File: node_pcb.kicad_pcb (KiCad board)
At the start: 2 copper layers, 27.9 x 52.1 mm, 22 parts, among them J1 EXT_PWR

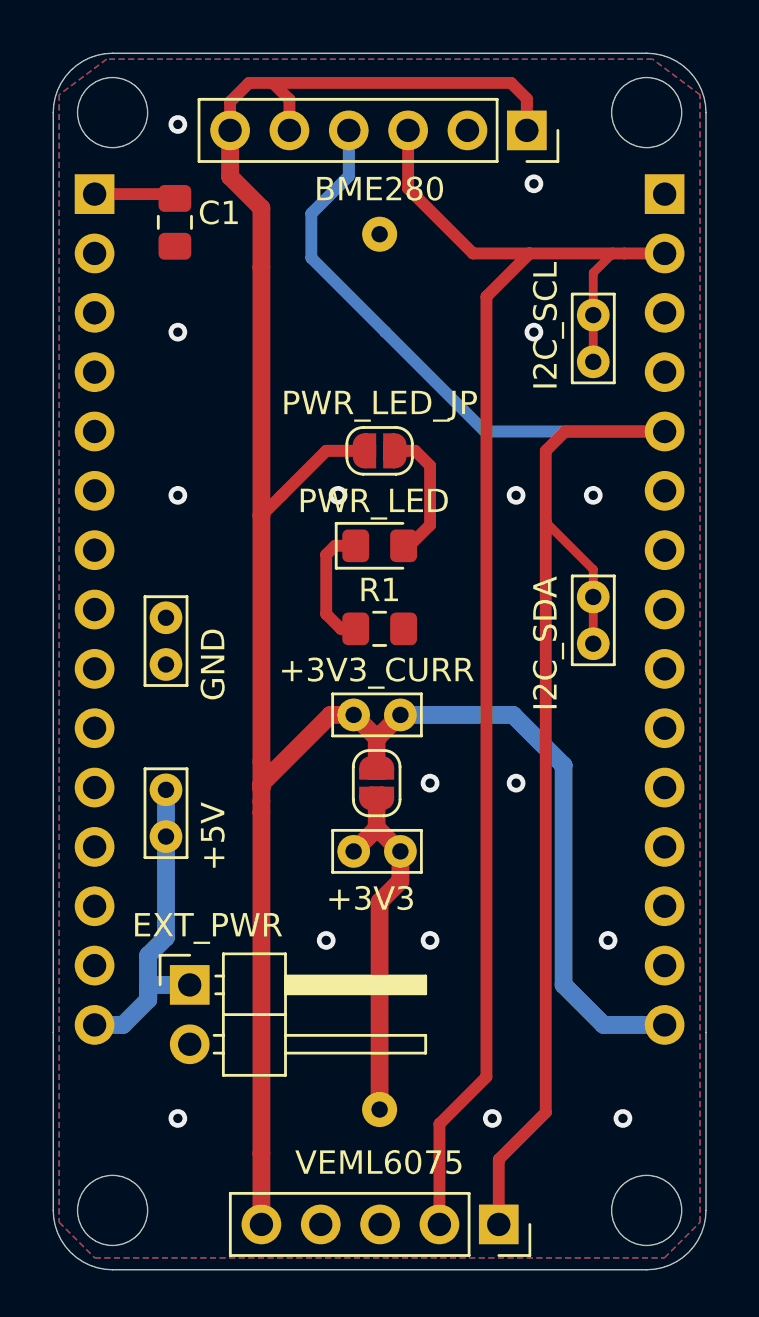
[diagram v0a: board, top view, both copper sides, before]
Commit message: dimensions fix
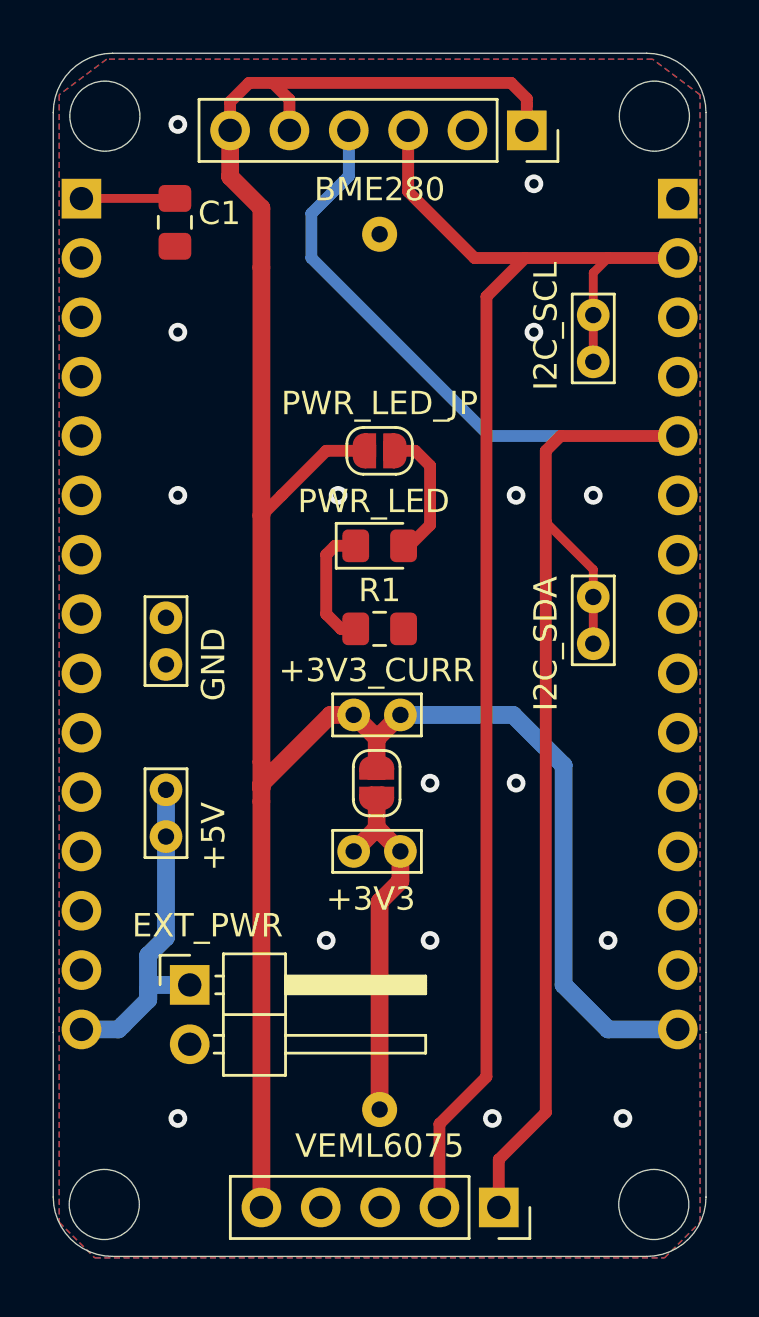
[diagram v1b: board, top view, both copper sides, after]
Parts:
- removed the REF** at (139.4, 101.1)
- removed the REF** at (162.3, 101.1)
- removed the REF** at (139.4, 54.1)
- added REF**: MountingHole_3mm, MountingHole:MountingHole_3mm, F.Cu at (139.1, 100.8)
- added REF**: MountingHole_3mm, MountingHole:MountingHole_3mm, F.Cu at (162.6, 100.8)
- added REF**: MountingHole_3mm, MountingHole:MountingHole_3mm, F.Cu at (139.1, 54.3)
- moved VEML6075 0.73 mm to (156.0, 101.0)
- moved ESP2 0.60 mm to (163.6, 57.8)
- moved ESP1 0.60 mm to (138.1, 57.8)
- moved REF** 0.36 mm to (162.6, 54.3)
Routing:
- net Net-(C1-Pad1): track 3.51 -> 4.26 mm
- net +5V: track 14.4 -> 15.0 mm
- net I2C_SCL: track 62.8 -> 62.2 mm
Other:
- board size 27.9 x 52.1 mm -> 27.9 x 51.5 mm

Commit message: bigger dimensions
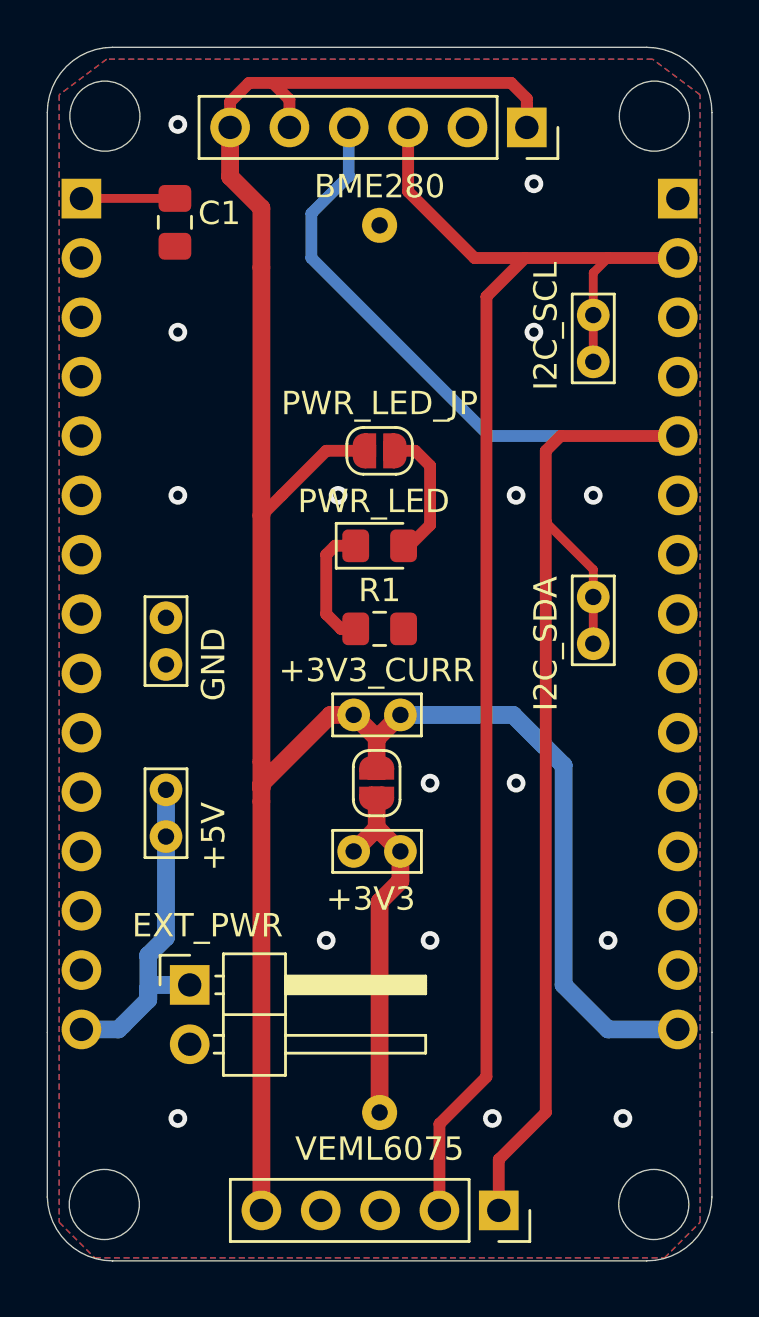
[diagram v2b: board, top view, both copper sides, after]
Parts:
- moved BAT-1 0.38 mm to (150.9, 58.9)
- moved BAT+1 0.13 mm to (150.9, 96.9)
- moved BME280 0.13 mm to (157.2, 54.7)
- moved VEML6075 0.13 mm to (156.0, 101.1)
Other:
- board size 27.9 x 51.5 mm -> 28.4 x 51.9 mm
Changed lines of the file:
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@@
   )
   (setup
-    (last_trace_width 0.508)
+    (last_trace_width 0.762)
     (user_trace_width 0.381)
     (user_trace_width 0.508)
@@
     (add_net "Net-(VEML6075-Pad4)")
   )
+  (module MountingHole:MountingHole_3mm (layer F.Cu)
+    (at 139.0904 100.838 180)
+    (descr "Mounting Hole 3mm, no annular")
+    (tags "mounting hole 3mm no annular")
+    (attr virtual)
+    (fp_text reference REF** (at 0 -4) (layer F.SilkS) hide
+      (effects (font (size 1 1) (thickness 0.15)))
+    )
+    (fp_text value MountingHole_3mm (at 0 4) (layer F.Fab)
+      (effects (font (size 1 1) (thickness 0.15)))
+    )
+    (fp_text user %R (at 0.3 0) (layer F.Fab)
+      (effects (font (size 1 1) (thickness 0.15)))
+    )
+    (fp_circle (center 0 0) (end 3 0) (layer Cmts.User) (width 0.15))
+    (fp_circle (center 0 0) (end 3.25 0) (layer F.CrtYd) (width 0.05))
+    (pad 1 np_thru_hole circle (at 0 0 180) (size 3 3) (drill 3) (layers *.Cu *.Mask))
+  )
   (module TestPoint:TestPoint_Bridge_Pitch2.0mm_Drill0.7mm (layer F.Cu)
     (at 141.732 77.724 90)
@@
   )
   (module MountingHole:MountingHole_3mm (layer F.Cu)
-    (at 139.0904 100.838 180)
-    (descr "Mounting Hole 3mm, no annular")
-    (tags "mounting hole 3mm no annular")
-    (attr virtual)
-    (fp_text reference REF** (at 0 -4) (layer F.SilkS) hide
-      (effects (font (size 1 1) (thickness 0.15)))
-    )
-    (fp_text value MountingHole_3mm (at 0 4) (layer F.Fab)
-      (effects (font (size 1 1) (thickness 0.15)))
-    )
-    (fp_text user %R (at 0.3 0) (layer F.Fab)
-      (effects (font (size 1 1) (thickness 0.15)))
-    )
-    (fp_circle (center 0 0) (end 3 0) (layer Cmts.User) (width 0.15))
-    (fp_circle (center 0 0) (end 3.25 0) (layer F.CrtYd) (width 0.05))
-    (pad 1 np_thru_hole circle (at 0 0 180) (size 3 3) (drill 3) (layers *.Cu *.Mask))
-  )
-  (module MountingHole:MountingHole_3mm (layer F.Cu)
     (at 162.6108 100.838 180)
     (descr "Mounting Hole 3mm, no annular")
@@
   )
   (module TestPoint:TestPoint_THTPad_D1.5mm_Drill0.7mm (layer B.Cu)
-    (at 150.876 59.309 180)
+    (at 150.876 58.928 180)
     (descr "THT pad as test Point, diameter 1.5mm, hole diameter 0.7mm")
     (tags "test point THT pad")
@@
   )
   (module TestPoint:TestPoint_THTPad_D1.5mm_Drill0.7mm (layer B.Cu)
-    (at 150.876 96.774 180)
+    (at 150.876 96.901 180)
     (descr "THT pad as test Point, diameter 1.5mm, hole diameter 0.7mm")
     (tags "test point THT pad")
@@
   )
   (module Connector_PinSocket_2.54mm:PinSocket_1x06_P2.54mm_Vertical (layer F.Cu)
-    (at 157.176 54.864 270)
+    (at 157.176 54.737 270)
     (descr "Through hole straight socket strip, 1x06, 2.54mm pitch, single row (from Kicad 4.0.7), script generated")
     (tags "Through hole socket strip THT 1x06 2.54mm single row")
@@
   )
   (module Connector_PinSocket_2.54mm:PinSocket_1x05_P2.54mm_Vertical (layer F.Cu)
-    (at 155.976 100.965 270)
+    (at 155.976 101.092 270)
     (descr "Through hole straight socket strip, 1x05, 2.54mm pitch, single row (from Kicad 4.0.7), script generated")
     (tags "Through hole socket strip THT 1x05 2.54mm single row")
@@
     )
   )
-  (gr_line (start 164.846 93.472) (end 164.846 100.5205) (layer Edge.Cuts) (width 0.05))
-  (gr_line (start 136.906 93.472) (end 136.906 100.5205) (layer Edge.Cuts) (width 0.05))
-  (gr_arc (start 139.446 100.5205) (end 136.906 100.5205) (angle -90) (layer Edge.Cuts) (width 0.05))
-  (gr_arc (start 162.306 100.5205) (end 162.306 103.0605) (angle -90) (layer Edge.Cuts) (width 0.05))
-  (gr_arc (start 162.306 54.102) (end 164.846 54.102) (angle -90) (layer Edge.Cuts) (width 0.05))
-  (gr_arc (start 139.446 54.102) (end 139.446 51.562) (angle -90) (layer Edge.Cuts) (width 0.05))
-  (gr_line (start 164.846 93.472) (end 164.846 54.102) (layer Edge.Cuts) (width 0.05))
-  (gr_line (start 139.446 103.0605) (end 162.306 103.0605) (layer Edge.Cuts) (width 0.05))
-  (gr_line (start 136.906 54.102) (end 136.906 93.472) (layer Edge.Cuts) (width 0.05))
-  (gr_line (start 162.306 51.562) (end 139.446 51.562) (layer Edge.Cuts) (width 0.05))
-  (segment (start 150.876 96.774) (end 150.876 87.884) (width 0.762) (layer F.Cu) (net 2))
+  (gr_arc (start 139.446 100.457) (end 136.652001 100.520499) (angle -88.69804733) (layer Edge.Cuts) (width 0.05))
+  (gr_arc (start 162.306 100.457) (end 162.306 103.251) (angle -88.69804733) (layer Edge.Cuts) (width 0.05))
+  (gr_arc (start 162.306 54.102) (end 165.1 54.102) (angle -90) (layer Edge.Cuts) (width 0.05))
+  (gr_arc (start 139.446 54.102) (end 139.446 51.308) (angle -90) (layer Edge.Cuts) (width 0.05))
+  (gr_line (start 165.1 93.472) (end 165.1 100.5205) (layer Edge.Cuts) (width 0.05))
+  (gr_line (start 136.652 93.472) (end 136.652 100.5205) (layer Edge.Cuts) (width 0.05))
+  (gr_line (start 165.1 93.472) (end 165.1 54.102) (layer Edge.Cuts) (width 0.05))
+  (gr_line (start 139.446 103.251) (end 162.306 103.251) (layer Edge.Cuts) (width 0.05))
+  (gr_line (start 136.652 54.102) (end 136.652 93.472) (layer Edge.Cuts) (width 0.05))
+  (gr_line (start 162.306 51.308) (end 139.446 51.308) (layer Edge.Cuts) (width 0.05))
   (segment (start 151.765 86.995) (end 150.876 87.884) (width 0.762) (layer F.Cu) (net 2))
   (segment (start 151.765 85.725) (end 151.765 86.995) (width 0.762) (layer F.Cu) (net 2))
@@
   (segment (start 150.749 84.741) (end 150.749 84.709) (width 0.762) (layer F.Cu) (net 2))
   (segment (start 149.765 85.725) (end 150.749 84.741) (width 0.762) (layer F.Cu) (net 2))
+  (segment (start 150.876 96.901) (end 150.876 87.884) (width 0.762) (layer F.Cu) (net 2))
   (via (at 155.702 97.155) (size 0.8) (drill 0.4) (layers F.Cu B.Cu) (net 3))
   (via (at 160.655 89.535) (size 0.8) (drill 0.4) (layers F.Cu B.Cu) (net 3))
